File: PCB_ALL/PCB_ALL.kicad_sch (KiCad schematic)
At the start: 41 parts, among them J1 Conn_01x02, J2 Conn_01x02, J3 Conn_01x01, J4 Conn_01x01, Q1 PNP, Q2 NJFET, Q3 Q_PUJT_BEB, U1 LM741, U2 NE555P, U3 NE555P

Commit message: Updated KiCAD project files
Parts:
- Ammeter+1: renamed from Ammeter+; footprint (none) -> Connector_PinHeader_2.54mm:PinHeader_1x01_P2.54mm_Vertical
- Ammeter-1: renamed from Ammeter-; footprint (none) -> Connector_PinHeader_2.54mm:PinHeader_1x01_P2.54mm_Vertical
- C1, C2, C3, C4: footprint (none) -> Capacitor_THT:C_Disc_D3.0mm_W2.0mm_P2.50mm
- Cap1, Cap2, J3, J4, Vbb1, Vbb2: footprint (none) -> Connector_PinHeader_2.54mm:PinHeader_1x01_P2.54mm_Vertical
- J1, J2: footprint (none) -> Connector_PinHeader_2.54mm:PinHeader_1x02_P2.54mm_Vertical
- Q1, Q2, Q3: footprint (none) -> Package_TO_SOT_THT:TO-92_HandSolder
- R1, R10, R11, R12, R2, R3, R4, R5, R6, R7, R8, R9: footprint (none) -> Resistor_THT:R_Axial_DIN0207_L6.3mm_D2.5mm_P7.62mm_Horizontal
- R_E1: renamed from R_E; footprint (none) -> Resistor_THT:R_Axial_DIN0207_L6.3mm_D2.5mm_P7.62mm_Horizontal
- Vdd+1: renamed from Vdd+; footprint (none) -> Connector_PinHeader_2.54mm:PinHeader_1x01_P2.54mm_Vertical
- Vdd-1: renamed from Vdd-; footprint (none) -> Connector_PinHeader_2.54mm:PinHeader_1x01_P2.54mm_Vertical
- Vgg+1: renamed from Vgg+; footprint (none) -> Connector_PinHeader_2.54mm:PinHeader_1x01_P2.54mm_Vertical
- Vgg-1: renamed from Vgg-; footprint (none) -> Connector_PinHeader_2.54mm:PinHeader_1x01_P2.54mm_Vertical
- Voltmeter+1, Voltmeter+2: renamed from Voltmeter+; footprint (none) -> Connector_PinHeader_2.54mm:PinHeader_1x01_P2.54mm_Vertical
- Voltmeter-1, Voltmeter-2: renamed from Voltmeter-; footprint (none) -> Connector_PinHeader_2.54mm:PinHeader_1x01_P2.54mm_Vertical
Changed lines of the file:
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@@
 			)
 		)
-		(property "Footprint" ""
+		(property "Footprint" "Package_TO_SOT_THT:TO-92_HandSolder"
 			(at 146.05 36.83 0)
 			(effects
@@
 			)
 		)
-		(property "Footprint" ""
+		(property "Footprint" "Resistor_THT:R_Axial_DIN0207_L6.3mm_D2.5mm_P7.62mm_Horizontal"
 			(at 118.11 41.148 90)
 			(effects
@@
 		(on_board yes)
 		(dnp no)
-		(property "Reference" "Ammeter+"
+		(property "Reference" "Ammeter+1"
 			(at 163.068 27.94 0)
 			(effects
@@
 			)
 		)
-		(property "Footprint" ""
+		(property "Footprint" "Connector_PinHeader_2.54mm:PinHeader_1x01_P2.54mm_Vertical"
 			(at 158.75 33.02 0)
 			(effects
@@
 			(project "PCB_ALL"
 				(path "/d7194cd2-1a83-4831-a32c-b5dd02c79ca9"
-					(reference "Ammeter+")
+					(reference "Ammeter+1")
 					(unit 1)
 				)
@@
 		(dnp no)
 		(fields_autoplaced yes)
-		(property "Reference" "Voltmeter-"
+		(property "Reference" "Voltmeter-2"
 			(at 168.91 53.3399 90)
 			(effects
@@
 			)
 		)
-		(property "Footprint" ""
+		(property "Footprint" "Connector_PinHeader_2.54mm:PinHeader_1x01_P2.54mm_Vertical"
 			(at 166.37 54.61 0)
 			(effects
@@
 			(project "PCB_ALL"
 				(path "/d7194cd2-1a83-4831-a32c-b5dd02c79ca9"
-					(reference "Voltmeter-")
+					(reference "Voltmeter-2")
 					(unit 1)
 				)
@@
 			)
 		)
-		(property "Footprint" ""
+		(property "Footprint" "Connector_PinHeader_2.54mm:PinHeader_1x01_P2.54mm_Vertical"
 			(at 125.73 116.84 0)
 			(effects
@@
 		(dnp no)
 		(fields_autoplaced yes)
-		(property "Reference" "Voltmeter+"
+		(property "Reference" "Voltmeter+2"
 			(at 168.91 48.2599 90)
 			(effects
@@
 			)
 		)
-		(property "Footprint" ""
+		(property "Footprint" "Connector_PinHeader_2.54mm:PinHeader_1x01_P2.54mm_Vertical"
 			(at 166.37 49.53 0)
 			(effects
@@
 			(project "PCB_ALL"
 				(path "/d7194cd2-1a83-4831-a32c-b5dd02c79ca9"
-					(reference "Voltmeter+")
+					(reference "Voltmeter+2")
 					(unit 1)
 				)
@@
 			)
 		)
-		(property "Footprint" ""
+		(property "Footprint" "Resistor_THT:R_Axial_DIN0207_L6.3mm_D2.5mm_P7.62mm_Horizontal"
 			(at 145.542 116.84 90)
 			(effects
@@
 			)
 		)
-		(property "Footprint" ""
+		(property "Footprint" "Resistor_THT:R_Axial_DIN0207_L6.3mm_D2.5mm_P7.62mm_Horizontal"
 			(at 127.508 92.71 90)
 			(effects
@@
 			)
 		)
-		(property "Footprint" ""
+		(property "Footprint" "Resistor_THT:R_Axial_DIN0207_L6.3mm_D2.5mm_P7.62mm_Horizontal"
 			(at 90.932 109.22 90)
 			(effects
@@
 			)
 		)
-		(property "Footprint" ""
+		(property "Footprint" "Resistor_THT:R_Axial_DIN0207_L6.3mm_D2.5mm_P7.62mm_Horizontal"
 			(at 145.542 92.71 90)
 			(effects
@@
 			)
 		)
-		(property "Footprint" ""
+		(property "Footprint" "Package_TO_SOT_THT:TO-92_HandSolder"
 			(at 115.57 165.1 0)
 			(effects
@@
 		(dnp no)
 		(fields_autoplaced yes)
-		(property "Reference" "Vgg-"
+		(property "Reference" "Vgg-1"
 			(at 110.49 44.4499 90)
 			(effects
@@
 			)
 		)
-		(property "Footprint" ""
+		(property "Footprint" "Connector_PinHeader_2.54mm:PinHeader_1x01_P2.54mm_Vertical"
 			(at 107.95 45.72 0)
 			(effects
@@
 			(project "PCB_ALL"
 				(path "/d7194cd2-1a83-4831-a32c-b5dd02c79ca9"
-					(reference "Vgg-")
+					(reference "Vgg-1")
 					(unit 1)
 				)
@@
 		(dnp no)
 		(fields_autoplaced yes)
-		(property "Reference" "Voltmeter+"
+		(property "Reference" "Voltmeter+1"
 			(at 128.27 44.4499 90)
 			(effects
@@
 			)
 		)
-		(property "Footprint" ""
+		(property "Footprint" "Connector_PinHeader_2.54mm:PinHeader_1x01_P2.54mm_Vertical"
 			(at 125.73 45.72 0)
 			(effects
@@
 			(project ""
 				(path "/d7194cd2-1a83-4831-a32c-b5dd02c79ca9"
-					(reference "Voltmeter+")
+					(reference "Voltmeter+1")
 					(unit 1)
 				)
@@
 		(on_board yes)
 		(dnp no)
-		(property "Reference" "Ammeter-"
+		(property "Reference" "Ammeter-1"
 			(at 142.748 28.194 0)
 			(effects
@@
 			)
 		)
-		(property "Footprint" ""
+		(property "Footprint" "Connector_PinHeader_2.54mm:PinHeader_1x01_P2.54mm_Vertical"
 			(at 152.4 33.02 0)
 			(effects
@@
 			(project "PCB_ALL"
 				(path "/d7194cd2-1a83-4831-a32c-b5dd02c79ca9"
-					(reference "Ammeter-")
+					(reference "Ammeter-1")
 					(unit 1)
 				)
@@
 			)
 		)
-		(property "Footprint" ""
+		(property "Footprint" "Capacitor_THT:C_Disc_D3.0mm_W2.0mm_P2.50mm"
 			(at 83.5152 187.96 0)
 			(effects
@@
 			)
 		)
-		(property "Footprint" ""
+		(property "Footprint" "Capacitor_THT:C_Disc_D3.0mm_W2.0mm_P2.50mm"
 			(at 30.1752 187.96 0)
 			(effects
@@
 			)
 		)
-		(property "Footprint" ""
+		(property "Footprint" "Resistor_THT:R_Axial_DIN0207_L6.3mm_D2.5mm_P7.62mm_Horizontal"
 			(at 123.952 100.33 90)
 			(effects
@@
 			)
 		)
-		(property "Footprint" ""
+		(property "Footprint" "Package_TO_SOT_THT:TO-92_HandSolder"
 			(at 149.86 101.6 0)
 			(effects
@@
 			)
 		)
-		(property "Footprint" ""
+		(property "Footprint" "Connector_PinHeader_2.54mm:PinHeader_1x01_P2.54mm_Vertical"
 			(at 158.75 110.49 0)
 			(effects
@@
 			)
 		)
-		(property "Footprint" ""
+		(property "Footprint" "Resistor_THT:R_Axial_DIN0207_L6.3mm_D2.5mm_P7.62mm_Horizontal"
 			(at 62.992 44.45 90)
 			(effects
@@
 		(dnp no)
 		(fields_autoplaced yes)
-		(property "Reference" "Voltmeter-"
+		(property "Reference" "Voltmeter-1"
 			(at 128.27 50.7999 90)
 			(effects
@@
 			)
 		)
-		(property "Footprint" ""
+		(property "Footprint" "Connector_PinHeader_2.54mm:PinHeader_1x01_P2.54mm_Vertical"
 			(at 125.73 52.07 0)
 			(effects
@@
 			(project "PCB_ALL"
 				(path "/d7194cd2-1a83-4831-a32c-b5dd02c79ca9"
-					(reference "Voltmeter-")
+					(reference "Voltmeter-1")
 					(unit 1)
 				)
@@
 		(on_board yes)
 		(dnp no)
-		(property "Reference" "Vdd-"
+		(property "Reference" "Vdd-1"
 			(at 187.452 61.976 0)
 			(effects
@@
 			)
 		)
-		(property "Footprint" ""
+		(property "Footprint" "Connector_PinHeader_2.54mm:PinHeader_1x01_P2.54mm_Vertical"
 			(at 185.42 54.61 0)
 			(effects
@@
 			(project "PCB_ALL"
 				(path "/d7194cd2-1a83-4831-a32c-b5dd02c79ca9"
-					(reference "Vdd-")
+					(reference "Vdd-1")
 					(unit 1)
 				)
@@
 		(dnp no)
 		(fields_autoplaced yes)
-		(property "Reference" "Vgg+"
+		(property "Reference" "Vgg+1"
 			(at 110.49 50.7999 90)
 			(effects
@@
 			)
 		)
-		(property "Footprint" ""
+		(property "Footprint" "Connector_PinHeader_2.54mm:PinHeader_1x01_P2.54mm_Vertical"
 			(at 107.95 52.07 0)
 			(effects
@@
 			(project "PCB_ALL"
 				(path "/d7194cd2-1a83-4831-a32c-b5dd02c79ca9"
-					(reference "Vgg+")
+					(reference "Vgg+1")
 					(unit 1)
 				)
@@
 			)
 		)
-		(property "Footprint" ""
+		(property "Footprint" "Connector_PinHeader_2.54mm:PinHeader_1x01_P2.54mm_Vertical"
 			(at 80.01 100.33 0)
 			(effects
@@
 			)
 		)
-		(property "Footprint" ""
+		(property "Footprint" "Connector_PinHeader_2.54mm:PinHeader_1x01_P2.54mm_Vertical"
 			(at 157.48 97.79 0)
 			(effects
@@
 			)
 		)
-		(property "Footprint" ""
+		(property "Footprint" "Resistor_THT:R_Axial_DIN0207_L6.3mm_D2.5mm_P7.62mm_Horizontal"
 			(at 69.342 160.02 90)
 			(effects
@@
 		(on_board yes)
 		(dnp no)
-		(property "Reference" "R_E"
+		(property "Reference" "R_E1"
 			(at 85.09 153.6699 0)
 			(effects
@@
 			)
 		)
-		(property "Footprint" ""
+		(property "Footprint" "Resistor_THT:R_Axial_DIN0207_L6.3mm_D2.5mm_P7.62mm_Horizontal"
 			(at 80.772 154.94 90)
 			(effects
@@
 			(project "PCB_ALL"
 				(path "/d7194cd2-1a83-4831-a32c-b5dd02c79ca9"
-					(reference "R_E")
+					(reference "R_E1")
 					(unit 1)
 				)
@@
 		(on_board yes)
 		(dnp no)
-		(property "Reference" "Vdd+"
+		(property "Reference" "Vdd+1"
 			(at 187.96 49.53 0)
 			(effects
@@
 			)
 		)
-		(property "Footprint" ""
+		(property "Footprint" "Connector_PinHeader_2.54mm:PinHeader_1x01_P2.54mm_Vertical"
 			(at 185.42 49.53 0)
 			(effects
@@
 			(project "PCB_ALL"
 				(path "/d7194cd2-1a83-4831-a32c-b5dd02c79ca9"
-					(reference "Vdd+")
+					(reference "Vdd+1")
 					(unit 1)
 				)
@@
 			)
 		)
-		(property "Footprint" ""
+		(property "Footprint" "Connector_PinHeader_2.54mm:PinHeader_1x02_P2.54mm_Vertical"
 			(at 88.9 40.64 0)
 			(effects
@@
 			)
 		)
-		(property "Footprint" ""
+		(property "Footprint" "Connector_PinHeader_2.54mm:PinHeader_1x02_P2.54mm_Vertical"
 			(at 24.13 38.1 0)
 			(effects
@@
 			)
 		)
-		(property "Footprint" ""
+		(property "Footprint" "Resistor_THT:R_Axial_DIN0207_L6.3mm_D2.5mm_P7.62mm_Horizontal"
 			(at 62.992 57.15 90)
 			(effects
@@
 			)
 		)
-		(property "Footprint" ""
+		(property "Footprint" "Connector_PinHeader_2.54mm:PinHeader_1x01_P2.54mm_Vertical"
 			(at 26.67 162.56 0)
 			(effects
@@
 			)
 		)
-		(property "Footprint" ""
+		(property "Footprint" "Connector_PinHeader_2.54mm:PinHeader_1x01_P2.54mm_Vertical"
 			(at 125.73 111.76 0)
 			(effects
@@
 			)
 		)
-		(property "Footprint" ""
+		(property "Footprint" "Resistor_THT:R_Axial_DIN0207_L6.3mm_D2.5mm_P7.62mm_Horizontal"
 			(at 173.99 34.798 90)
 			(effects
@@
 			)
 		)
-		(property "Footprint" ""
+		(property "Footprint" "Capacitor_THT:C_Disc_D3.0mm_W2.0mm_P2.50mm"
 			(at 36.5252 113.03 0)
 			(effects
@@
 			)
 		)
-		(property "Footprint" ""
+		(property "Footprint" "Resistor_THT:R_Axial_DIN0207_L6.3mm_D2.5mm_P7.62mm_Horizontal"
 			(at 90.932 101.6 90)
 			(effects
@@
 			)
 		)
-		(property "Footprint" ""
+		(property "Footprint" "Capacitor_THT:C_Disc_D3.0mm_W2.0mm_P2.50mm"
 			(at 26.3652 113.03 0)
 			(effects
@@
 			)
 		)
-		(property "Footprint" ""
+		(property "Footprint" "Resistor_THT:R_Axial_DIN0207_L6.3mm_D2.5mm_P7.62mm_Horizontal"
 			(at 69.342 170.18 90)
 			(effects

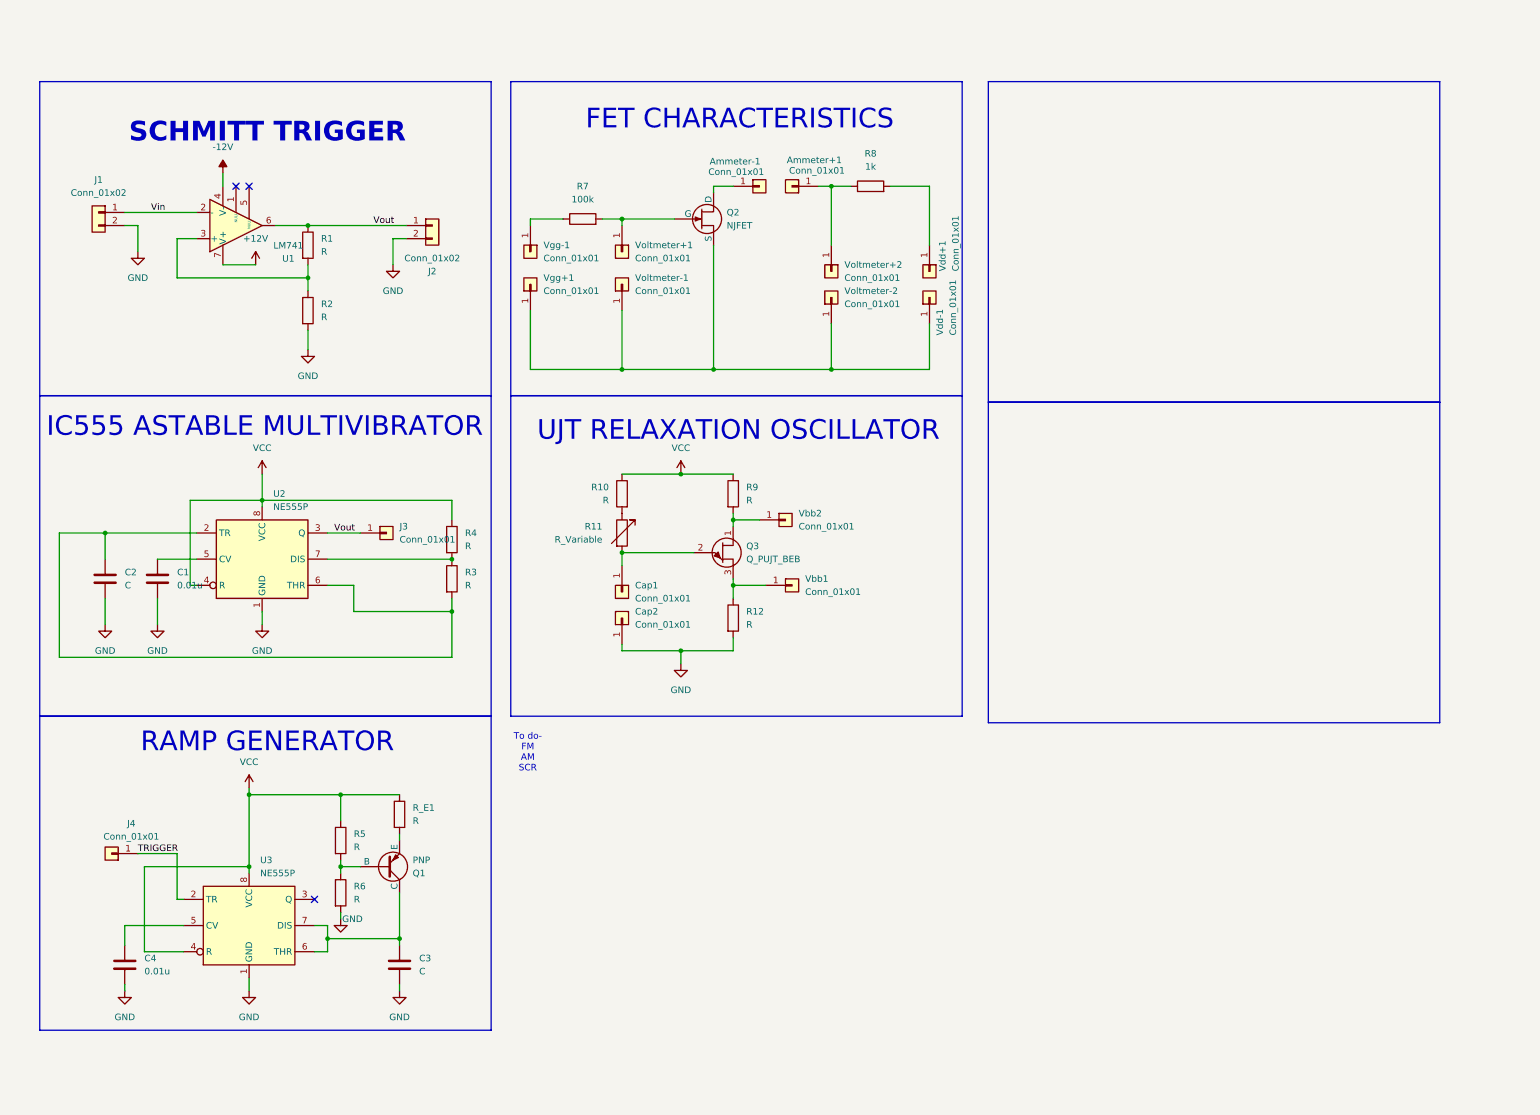
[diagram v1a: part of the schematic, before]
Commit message: Updated KiCAD schematic and PCB layout
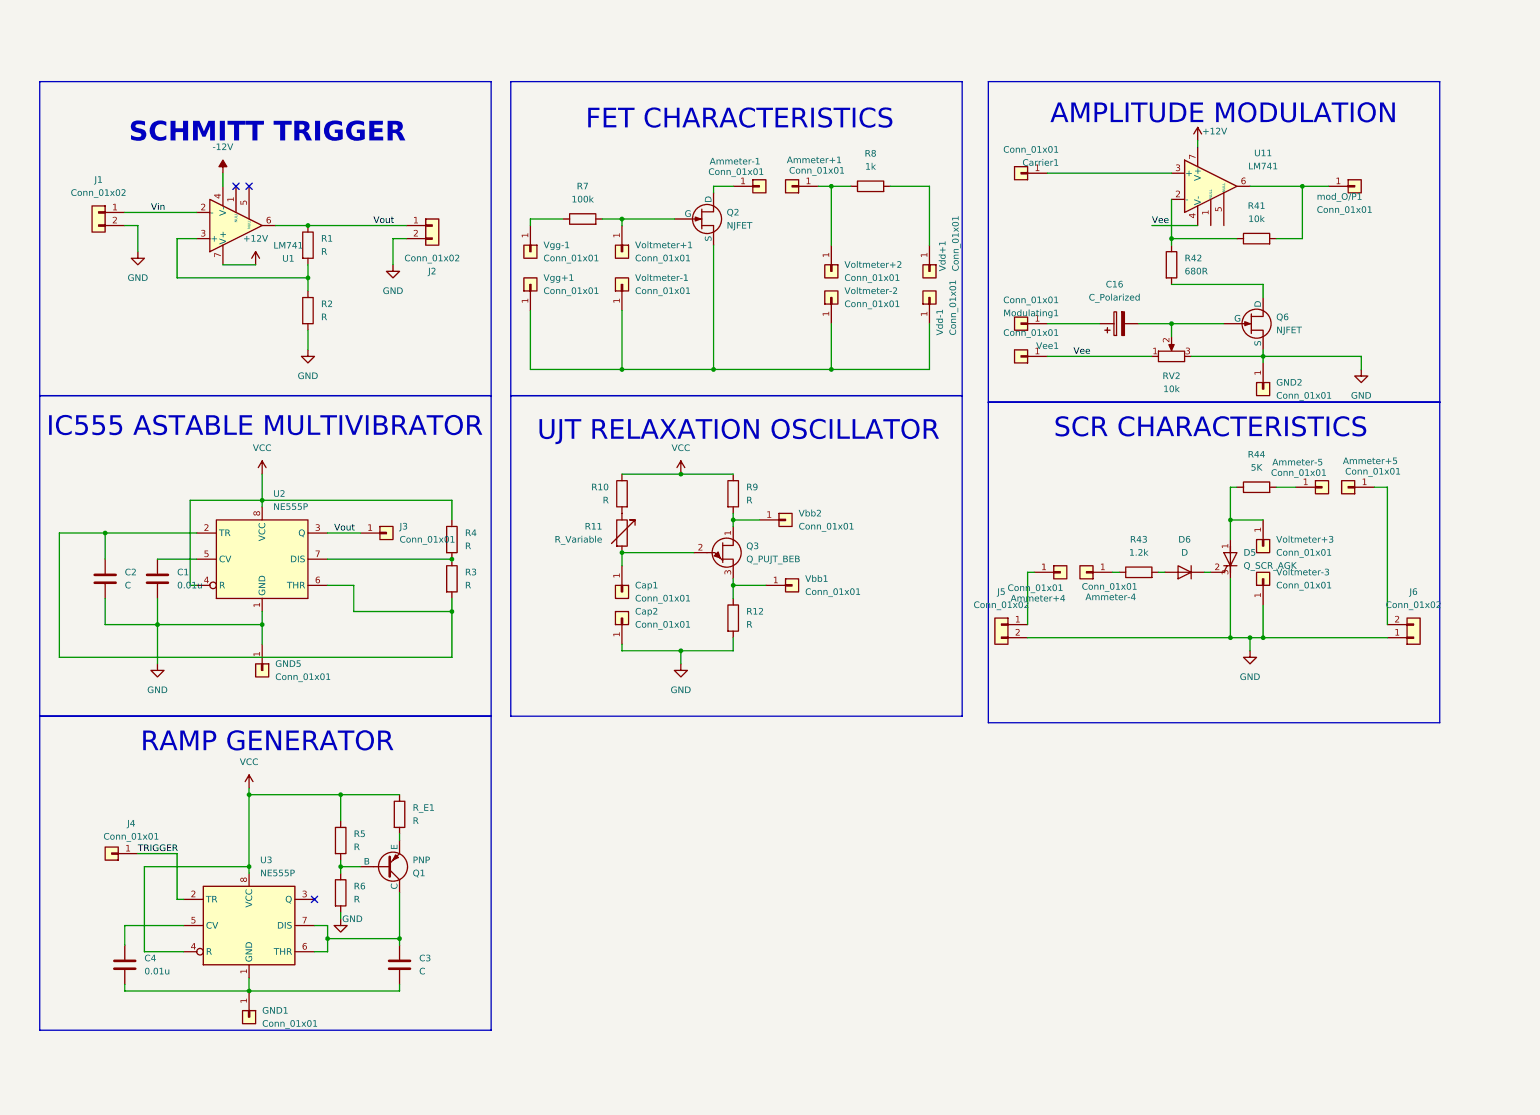
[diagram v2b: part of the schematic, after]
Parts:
- added Ammeter+4, Ammeter+5, Ammeter-4, Ammeter-5, Carrier1, GND1, GND2, GND5, Modulating1, Vee1, Voltmeter+3, Voltmeter-3, mod_O/P1: Conn_01x01, Connector_PinSocket_2.54mm:PinSocket_1x01_P2.54mm_Vertical, symbol Connector_Generic:Conn_01x01
- added C16: C_Polarized, Capacitor_THT:CP_Radial_D5.0mm_P2.50mm, symbol Device:C_Polarized
- added D5: Q_SCR_AGK, Package_TO_SOT_THT:TO-92, symbol Device:Q_SCR_AGK
- added D6: D, Diode_SMD:D_0805_2012Metric, symbol Device:D
- added J5, J6: Conn_01x02, Connector_PinSocket_2.54mm:PinSocket_1x02_P2.54mm_Vertical, symbol Connector_Generic:Conn_01x02
- added Q6: NJFET, Package_TO_SOT_SMD:SOT-23, symbol Simulation_SPICE:NJFET
- added R41: 10k, Resistor_SMD:R_0805_2012Metric_Pad1.20x1.40mm_HandSolder, symbol Device:R
- added R42: 680R, Resistor_SMD:R_0805_2012Metric_Pad1.20x1.40mm_HandSolder, symbol Device:R
- added R43: 1.2k, Resistor_SMD:R_0805_2012Metric_Pad1.20x1.40mm_HandSolder, symbol Device:R
- added R44: 5K, Resistor_SMD:R_0805_2012Metric_Pad1.20x1.40mm_HandSolder, symbol Device:R
- added RV2: 10k, Potentiometer_THT:Potentiometer_Bourns_3296P_Horizontal, symbol Device:R_Potentiometer
- added U11: LM741, Package_SO:SOIC-8_3.9x4.9mm_P1.27mm, symbol Amplifier_Operational:LM741
- Ammeter+1, Ammeter-1, Cap1, Cap2, J3, J4, Vbb1, Vbb2, Vdd+1, Vdd-1, Vgg+1, Vgg-1, Voltmeter+1, Voltmeter+2, Voltmeter-1, Voltmeter-2: footprint Connector_PinHeader_2.54mm:PinHeader_1x01_P2.54mm_Vertical -> Connector_PinSocket_2.54mm:PinSocket_1x01_P2.54mm_Vertical
- C1, C2, C3, C4: footprint Capacitor_THT:C_Disc_D3.0mm_W2.0mm_P2.50mm -> Capacitor_SMD:C_0805_2012Metric_Pad1.18x1.45mm_HandSolder
- J1, J2: footprint Connector_PinHeader_2.54mm:PinHeader_1x02_P2.54mm_Vertical -> Connector_PinSocket_2.54mm:PinSocket_1x02_P2.54mm_Vertical
- R1, R10, R12, R2, R3, R4, R5, R6, R7, R8, R9: footprint Resistor_THT:R_Axial_DIN0207_L6.3mm_D2.5mm_P7.62mm_Horizontal -> Resistor_SMD:R_0805_2012Metric_Pad1.20x1.40mm_HandSolder
- U1: footprint Package_DIP:DIP-8_W7.62mm_Socket -> Package_SO:SOIC-8_3.9x4.9mm_P1.27mm
- U2, U3: footprint Package_DIP:DIP-8_W7.62mm -> Package_SO:SOIC-8_3.9x4.9mm_P1.27mm
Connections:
- net +12V: now also U11.7 (V+)
- net GND: now also D5.3 (K), GND2.1 (Pin_1), GND5.1 (Pin_1), J5.2 (Pin_2), J6.1 (Pin_1), Q6.3 (S), RV2.3, Voltmeter-3.1 (Pin_1); no longer C3.2, C4.2, U3.1 (GND)
- new net: D5.2 (G), D6.1 (K)
- new net: D6.2 (A), R43.2
- new net: Carrier1.1 (Pin_1), U11.3 (+)
- new net: R41.1, R42.1, U11.2 (-)
- new net: Q6.1 (D), R42.2
- new net: C3.2, C4.2, GND1.1 (Pin_1), U3.1 (GND)
- new net: Ammeter-4.1 (Pin_1), R43.1
- new net: C16.2, Q6.2 (G), RV2.2
- new net: Ammeter-5.1 (Pin_1), R44.2
- new net: D5.1 (A), R44.1, Voltmeter+3.1 (Pin_1)
- new net: R41.2, U11.6, mod_O/P1.1 (Pin_1)
- new net: Ammeter+4.1 (Pin_1), J5.1 (Pin_1)
- new net: Ammeter+5.1 (Pin_1), J6.2 (Pin_2)
- new net: C16.1, Modulating1.1 (Pin_1)
- new net Vee: RV2.1, U11.4 (V-), Vee1.1 (Pin_1)
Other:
- note added: "AMPLITUDE MODULATION"
- note added: "SCR CHARACTERISTICS"
- note removed: "To do- FM AM SCR"
